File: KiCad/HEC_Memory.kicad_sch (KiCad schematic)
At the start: 11 parts, among them U13 74LS245, U14 74LS245, U15 74LS32, U16 74LS32, U2 AS6C4008-55PCN, U22 74LS02, U3 AS6C4008-55PCN, U4 CY7C199, U41 74LS02, U5 CY7C199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

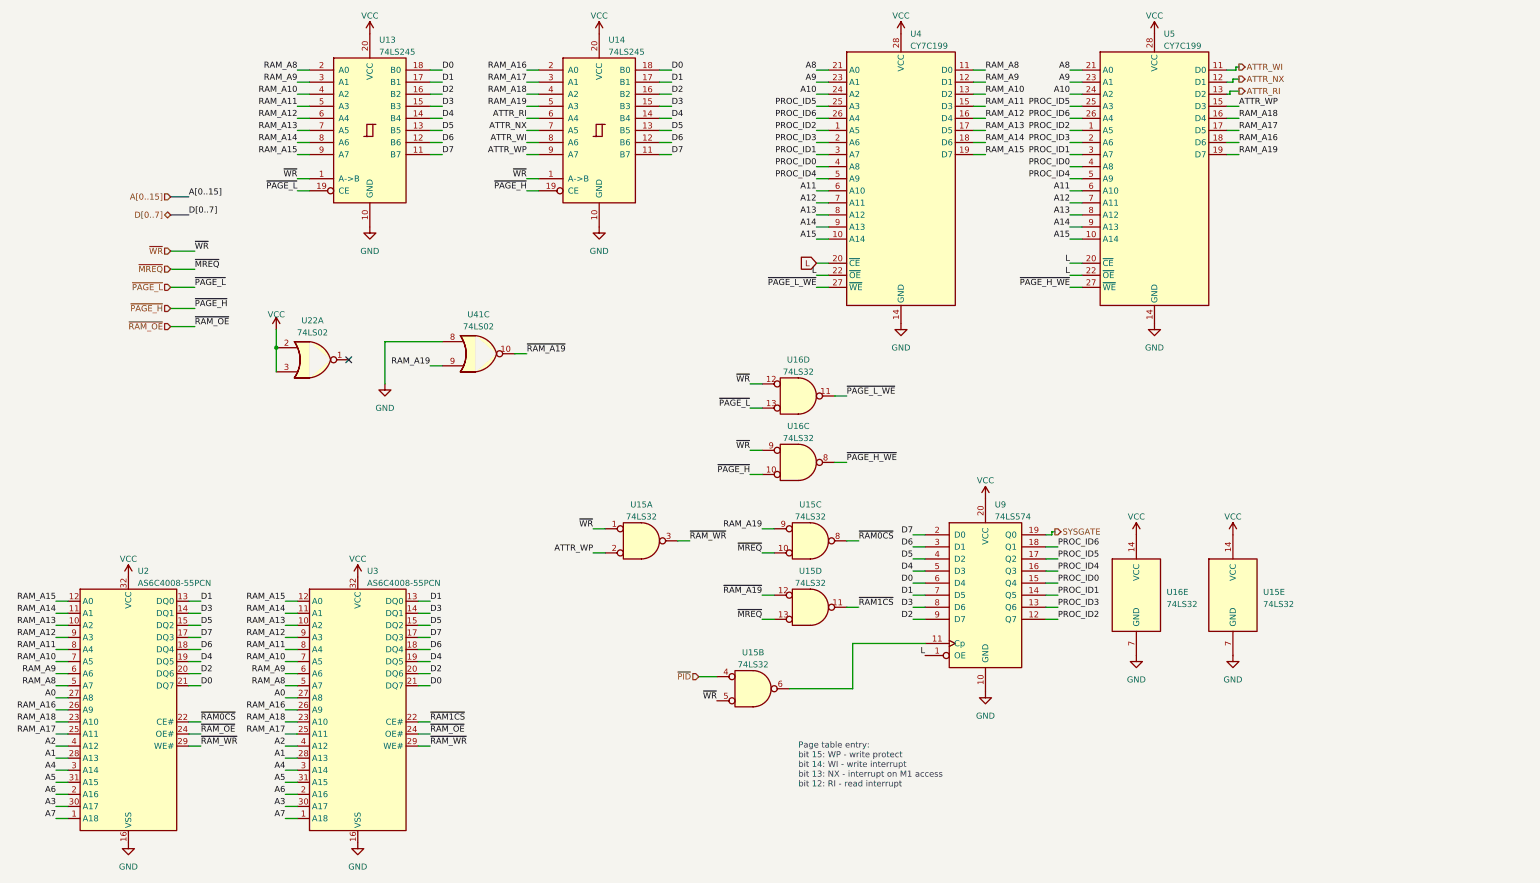
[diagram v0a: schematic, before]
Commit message: Bottom left routing complete
Finished routing the bottom left side of the PCB (wait generation and part of protection). Minor changes to schematic to ease routing.
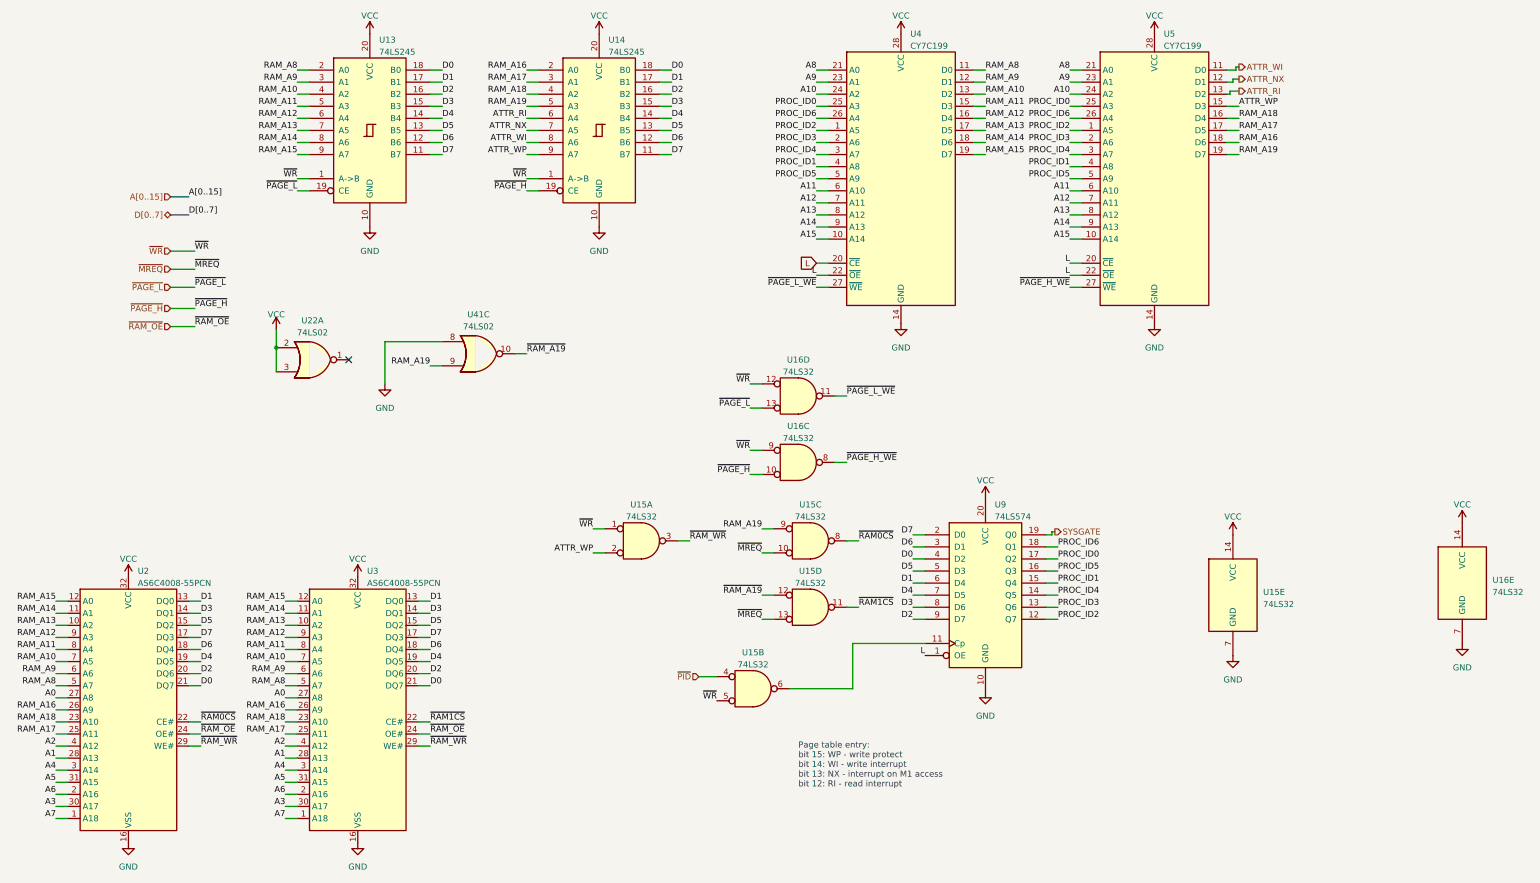
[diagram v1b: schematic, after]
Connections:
- net D0: now also U9.4 (D2); no longer U9.6 (D4)
- net D1: now also U9.6 (D4); no longer U9.7 (D5)
- net D4: now also U9.7 (D5); no longer U9.5 (D3)
- net D5: now also U9.5 (D3); no longer U9.4 (D2)
- net PROC_ID0: now also U4.25 (A3), U5.25 (A3), U9.17 (Q2); no longer U4.4 (A8), U5.4 (A8), U9.15 (Q4)
- net PROC_ID1: now also U4.4 (A8), U5.4 (A8), U9.15 (Q4); no longer U4.3 (A7), U5.3 (A7), U9.14 (Q5)
- net PROC_ID4: now also U4.3 (A7), U5.3 (A7), U9.14 (Q5); no longer U4.5 (A9), U5.5 (A9), U9.16 (Q3)
- net PROC_ID5: now also U4.5 (A9), U5.5 (A9), U9.16 (Q3); no longer U4.25 (A3), U5.25 (A3), U9.17 (Q2)
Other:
- moved on the sheet: U16E
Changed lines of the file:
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@@
     (effects (font (size 1.27 1.27)) (justify left bottom))
   )
-  (label "D4" (at 203.2 133.35 180) (fields_autoplaced)
+  (label "D4" (at 203.2 138.43 180) (fields_autoplaced)
     (effects (font (size 1.27 1.27)) (justify right bottom))
   )
@@
     (effects (font (size 1.27 1.27)) (justify right bottom))
   )
-  (label "D1" (at 203.2 138.43 180) (fields_autoplaced)
+  (label "D1" (at 203.2 135.89 180) (fields_autoplaced)
     (effects (font (size 1.27 1.27)) (justify right bottom))
   )
@@
     (effects (font (size 1.27 1.27)) (justify right bottom))
   )
-  (label "PROC_ID1" (at 233.68 138.43 0) (fields_autoplaced)
+  (label "PROC_ID1" (at 233.68 135.89 0) (fields_autoplaced)
     (effects (font (size 1.27 1.27)) (justify left bottom))
   )
@@
     (effects (font (size 1.27 1.27)) (justify left bottom))
   )
-  (label "PROC_ID4" (at 233.68 133.35 0) (fields_autoplaced)
+  (label "PROC_ID4" (at 233.68 138.43 0) (fields_autoplaced)
     (effects (font (size 1.27 1.27)) (justify left bottom))
   )
@@
     (effects (font (size 1.27 1.27)) (justify left bottom))
   )
-  (label "PROC_ID5" (at 233.68 130.81 0) (fields_autoplaced)
+  (label "PROC_ID5" (at 233.68 133.35 0) (fields_autoplaced)
     (effects (font (size 1.27 1.27)) (justify left bottom))
   )
@@
     (effects (font (size 1.27 1.27)) (justify right bottom))
   )
-  (label "PROC_ID5" (at 236.22 35.56 180) (fields_autoplaced)
+  (label "PROC_ID5" (at 236.22 50.8 180) (fields_autoplaced)
     (effects (font (size 1.27 1.27)) (justify right bottom))
   )
@@
     (effects (font (size 1.27 1.27)) (justify right bottom))
   )
-  (label "PROC_ID4" (at 236.22 50.8 180) (fields_autoplaced)
+  (label "PROC_ID4" (at 236.22 45.72 180) (fields_autoplaced)
     (effects (font (size 1.27 1.27)) (justify right bottom))
   )
@@
     (effects (font (size 1.27 1.27)) (justify left bottom))
   )
-  (label "D0" (at 203.2 135.89 180) (fields_autoplaced)
+  (label "D0" (at 203.2 130.81 180) (fields_autoplaced)
     (effects (font (size 1.27 1.27)) (justify right bottom))
   )
@@
     (effects (font (size 1.27 1.27)) (justify right bottom))
   )
-  (label "PROC_ID1" (at 236.22 45.72 180) (fields_autoplaced)
+  (label "PROC_ID1" (at 236.22 48.26 180) (fields_autoplaced)
     (effects (font (size 1.27 1.27)) (justify right bottom))
   )
@@
     (effects (font (size 1.27 1.27)) (justify left bottom))
   )
-  (label "PROC_ID1" (at 182.88 45.72 180) (fields_autoplaced)
+  (label "PROC_ID1" (at 182.88 48.26 180) (fields_autoplaced)
     (effects (font (size 1.27 1.27)) (justify right bottom))
   )
@@
     (effects (font (size 1.27 1.27)) (justify right bottom))
   )
-  (label "PROC_ID5" (at 182.88 35.56 180) (fields_autoplaced)
+  (label "PROC_ID5" (at 182.88 50.8 180) (fields_autoplaced)
     (effects (font (size 1.27 1.27)) (justify right bottom))
   )
@@
     (effects (font (size 1.27 1.27)) (justify right bottom))
   )
-  (label "PROC_ID0" (at 236.22 48.26 180) (fields_autoplaced)
+  (label "PROC_ID0" (at 236.22 35.56 180) (fields_autoplaced)
     (effects (font (size 1.27 1.27)) (justify right bottom))
   )
@@
     (effects (font (size 1.27 1.27)) (justify left bottom))
   )
-  (label "PROC_ID4" (at 182.88 50.8 180) (fields_autoplaced)
+  (label "PROC_ID4" (at 182.88 45.72 180) (fields_autoplaced)
     (effects (font (size 1.27 1.27)) (justify right bottom))
   )
@@
     (effects (font (size 1.27 1.27)) (justify right bottom))
   )
-  (label "PROC_ID0" (at 233.68 135.89 0) (fields_autoplaced)
+  (label "PROC_ID0" (at 233.68 130.81 0) (fields_autoplaced)
     (effects (font (size 1.27 1.27)) (justify left bottom))
   )
@@
     (effects (font (size 1.27 1.27)) (justify left bottom))
   )
-  (label "PROC_ID0" (at 182.88 48.26 180) (fields_autoplaced)
-    (effects (font (size 1.27 1.27)) (justify right bottom))
-  )
-  (label "D5" (at 203.2 130.81 180) (fields_autoplaced)
+  (label "PROC_ID0" (at 182.88 35.56 180) (fields_autoplaced)
+    (effects (font (size 1.27 1.27)) (justify right bottom))
+  )
+  (label "D5" (at 203.2 133.35 180) (fields_autoplaced)
     (effects (font (size 1.27 1.27)) (justify right bottom))
   )
@@
     )
   )
-  (symbol (lib_id "power:GND") (at 250.19 151.13 0) (unit 1)
-    (in_bom yes) (on_board yes) (dnp no) (fields_autoplaced)
-    (property "Reference" "#PWR022" (at 250.19 157.48 0)
-      (effects (font (size 1.27 1.27)) hide)
-    )
-    (property "Value" "GND" (at 250.19 156.21 0)
-      (effects (font (size 1.27 1.27)))
-    )
-    (property "Footprint" "" (at 250.19 151.13 0)
-      (effects (font (size 1.27 1.27)) hide)
-    )
-    (property "Datasheet" "" (at 250.19 151.13 0)
+  (symbol (lib_id "power:GND") (at 318.77 148.59 0) (unit 1)
+    (in_bom yes) (on_board yes) (dnp no) (fields_autoplaced)
+    (property "Reference" "#PWR022" (at 318.77 154.94 0)
+      (effects (font (size 1.27 1.27)) hide)
+    )
+    (property "Value" "GND" (at 318.77 153.67 0)
+      (effects (font (size 1.27 1.27)))
+    )
+    (property "Footprint" "" (at 318.77 148.59 0)
+      (effects (font (size 1.27 1.27)) hide)
+    )
+    (property "Datasheet" "" (at 318.77 148.59 0)
       (effects (font (size 1.27 1.27)) hide)
     )
@@
     )
   )
-  (symbol (lib_id "power:VCC") (at 250.19 125.73 0) (unit 1)
-    (in_bom yes) (on_board yes) (dnp no) (fields_autoplaced)
-    (property "Reference" "#PWR021" (at 250.19 129.54 0)
-      (effects (font (size 1.27 1.27)) hide)
-    )
-    (property "Value" "VCC" (at 250.19 121.92 0)
-      (effects (font (size 1.27 1.27)))
-    )
-    (property "Footprint" "" (at 250.19 125.73 0)
-      (effects (font (size 1.27 1.27)) hide)
-    )
-    (property "Datasheet" "" (at 250.19 125.73 0)
+  (symbol (lib_id "power:VCC") (at 318.77 123.19 0) (unit 1)
+    (in_bom yes) (on_board yes) (dnp no) (fields_autoplaced)
+    (property "Reference" "#PWR021" (at 318.77 127 0)
+      (effects (font (size 1.27 1.27)) hide)
+    )
+    (property "Value" "VCC" (at 318.77 119.38 0)
+      (effects (font (size 1.27 1.27)))
+    )
+    (property "Footprint" "" (at 318.77 123.19 0)
+      (effects (font (size 1.27 1.27)) hide)
+    )
+    (property "Datasheet" "" (at 318.77 123.19 0)
       (effects (font (size 1.27 1.27)) hide)
     )
@@
     )
   )
-  (symbol (lib_id "74xx:74LS32") (at 250.19 138.43 0) (unit 5)
-    (in_bom yes) (on_board yes) (dnp no) (fields_autoplaced)
-    (property "Reference" "U16" (at 256.54 137.795 0)
+  (symbol (lib_id "74xx:74LS32") (at 318.77 135.89 0) (unit 5)
+    (in_bom yes) (on_board yes) (dnp no) (fields_autoplaced)
+    (property "Reference" "U16" (at 325.12 135.255 0)
       (effects (font (size 1.27 1.27)) (justify left))
     )
-    (property "Value" "74LS32" (at 256.54 140.335 0)
+    (property "Value" "74LS32" (at 325.12 137.795 0)
       (effects (font (size 1.27 1.27)) (justify left))
     )
-    (property "Footprint" "Package_DIP:DIP-14_W7.62mm_Socket" (at 250.19 138.43 0)
-      (effects (font (size 1.27 1.27)) hide)
-    )
-    (property "Datasheet" "http://www.ti.com/lit/gpn/sn74LS32" (at 250.19 138.43 0)
-      (effects (font (size 1.27 1.27)) hide)
-    )
+    (property "Footprint" "Package_DIP:DIP-14_W7.62mm_Socket" (at 318.77 135.89 0)
+      (effects (font (size 1.27 1.27)) hide)
+    )
+    (property "Datasheet" "http://www.ti.com/lit/gpn/sn74LS32" (at 318.77 135.89 0)
+      (effects (font (size 1.27 1.27)) hide)
+    )

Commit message: Preliminary routing
Changed footprint pad size to allow 2 traces to be routed between adjacent pads. Finished routing all ICs. Bypass caps not added. Some traces may need to be optimized.
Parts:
- U13, U14, U9: footprint Package_DIP:DIP-20_W7.62mm_Socket -> Library:DIP-20_W7.62mm_Socket_ThinPads
- U15, U16, U22, U41: footprint Package_DIP:DIP-14_W7.62mm_Socket -> Library:DIP-14_W7.62mm_Socket_ThinPads
- U2, U3: footprint Package_DIP:DIP-32_W15.24mm_Socket -> Library:DIP-32_W15.24mm_Socket_ThinPads
- U4, U5: footprint Package_DIP:DIP-28_W7.62mm_Socket -> Library:DIP-28_W7.62mm_Socket_ThinPads
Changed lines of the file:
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@@
       (effects (font (size 1.27 1.27)) (justify left))
     )
-    (property "Footprint" "Package_DIP:DIP-14_W7.62mm_Socket" (at 270.51 138.43 0)
+    (property "Footprint" "Library:DIP-14_W7.62mm_Socket_ThinPads" (at 270.51 138.43 0)
       (effects (font (size 1.27 1.27)) hide)
     )
@@
       (effects (font (size 1.27 1.27)) (justify left))
     )
-    (property "Footprint" "Package_DIP:DIP-32_W15.24mm_Socket" (at 38.1 160.02 0)
+    (property "Footprint" "Library:DIP-32_W15.24mm_Socket_ThinPads" (at 38.1 160.02 0)
       (effects (font (size 1.27 1.27)) hide)
     )
@@
       (effects (font (size 1.27 1.27)))
     )
-    (property "Footprint" "Package_DIP:DIP-14_W7.62mm_Socket" (at 179.07 96.52 0)
+    (property "Footprint" "Library:DIP-14_W7.62mm_Socket_ThinPads" (at 179.07 96.52 0)
       (effects (font (size 1.27 1.27)) hide)
     )
@@
       (effects (font (size 1.27 1.27)) (justify left))
     )
-    (property "Footprint" "Package_DIP:DIP-28_W7.62mm_Socket" (at 200.66 50.8 0)
+    (property "Footprint" "Library:DIP-28_W7.62mm_Socket_ThinPads" (at 200.66 50.8 0)
       (effects (font (size 1.27 1.27)) hide)
     )
@@
       (effects (font (size 1.27 1.27)))
     )
-    (property "Footprint" "Package_DIP:DIP-14_W7.62mm_Socket" (at 179.07 110.49 0)
+    (property "Footprint" "Library:DIP-14_W7.62mm_Socket_ThinPads" (at 179.07 110.49 0)
       (effects (font (size 1.27 1.27)) hide)
     )
@@
       (effects (font (size 1.27 1.27)) (justify left))
     )
-    (property "Footprint" "Package_DIP:DIP-32_W15.24mm_Socket" (at 86.36 160.02 0)
+    (property "Footprint" "Library:DIP-32_W15.24mm_Socket_ThinPads" (at 86.36 160.02 0)
       (effects (font (size 1.27 1.27)) hide)
     )
@@
       (effects (font (size 1.27 1.27)) (justify left))
     )
-    (property "Footprint" "Package_DIP:DIP-28_W7.62mm_Socket" (at 254 50.8 0)
+    (property "Footprint" "Library:DIP-28_W7.62mm_Socket_ThinPads" (at 254 50.8 0)
       (effects (font (size 1.27 1.27)) hide)
     )
@@
       (effects (font (size 1.27 1.27)))
     )
-    (property "Footprint" "Package_DIP:DIP-14_W7.62mm_Socket" (at 76.835 88.9 0)
+    (property "Footprint" "Library:DIP-14_W7.62mm_Socket_ThinPads" (at 76.835 88.9 0)
       (effects (font (size 1.27 1.27)) hide)
     )
@@
       (effects (font (size 1.27 1.27)))
     )
-    (property "Footprint" "Package_DIP:DIP-14_W7.62mm_Socket" (at 181.61 127 0)
+    (property "Footprint" "Library:DIP-14_W7.62mm_Socket_ThinPads" (at 181.61 127 0)
       (effects (font (size 1.27 1.27)) hide)
     )
@@
       (effects (font (size 1.27 1.27)))
     )
-    (property "Footprint" "Package_DIP:DIP-14_W7.62mm_Socket" (at 169.545 158.115 0)
+    (property "Footprint" "Library:DIP-14_W7.62mm_Socket_ThinPads" (at 169.545 158.115 0)
       (effects (font (size 1.27 1.27)) hide)
     )
@@
       (effects (font (size 1.27 1.27)))
     )
-    (property "Footprint" "Package_DIP:DIP-14_W7.62mm_Socket" (at 111.76 87.63 0)
+    (property "Footprint" "Library:DIP-14_W7.62mm_Socket_ThinPads" (at 111.76 87.63 0)
       (effects (font (size 1.27 1.27)) hide)
     )
@@
       (effects (font (size 1.27 1.27)) (justify left))
     )
-    (property "Footprint" "Package_DIP:DIP-20_W7.62mm_Socket" (at 137.16 40.64 0)
+    (property "Footprint" "Library:DIP-20_W7.62mm_Socket_ThinPads" (at 137.16 40.64 0)
       (effects (font (size 1.27 1.27)) hide)
     )
@@
       (effects (font (size 1.27 1.27)))
     )
-    (property "Footprint" "Package_DIP:DIP-14_W7.62mm_Socket" (at 181.61 140.97 0)
+    (property "Footprint" "Library:DIP-14_W7.62mm_Socket_ThinPads" (at 181.61 140.97 0)
       (effects (font (size 1.27 1.27)) hide)
     )
@@
       (effects (font (size 1.27 1.27)) (justify left))
     )
-    (property "Footprint" "Package_DIP:DIP-20_W7.62mm_Socket" (at 88.9 40.64 0)
+    (property "Footprint" "Library:DIP-20_W7.62mm_Socket_ThinPads" (at 88.9 40.64 0)
       (effects (font (size 1.27 1.27)) hide)
     )
@@
       (effects (font (size 1.27 1.27)) (justify left))
     )
-    (property "Footprint" "Package_DIP:DIP-20_W7.62mm_Socket" (at 218.44 138.43 0)
+    (property "Footprint" "Library:DIP-20_W7.62mm_Socket_ThinPads" (at 218.44 138.43 0)
       (effects (font (size 1.27 1.27)) hide)
     )
@@
       (effects (font (size 1.27 1.27)))
     )
-    (property "Footprint" "Package_DIP:DIP-14_W7.62mm_Socket" (at 146.05 127 0)
+    (property "Footprint" "Library:DIP-14_W7.62mm_Socket_ThinPads" (at 146.05 127 0)
       (effects (font (size 1.27 1.27)) hide)
     )
@@
       (effects (font (size 1.27 1.27)) (justify left))
     )
-    (property "Footprint" "Package_DIP:DIP-14_W7.62mm_Socket" (at 318.77 135.89 0)
-      (effects (font (size 1.27 1.27)) hide)
-    )
+    (property "Footprint" "Library:DIP-14_W7.62mm_Socket_ThinPads" (at 318.77 135.89 0)
+      (effects (font (size 1.27 1.27)) hide)
+    )

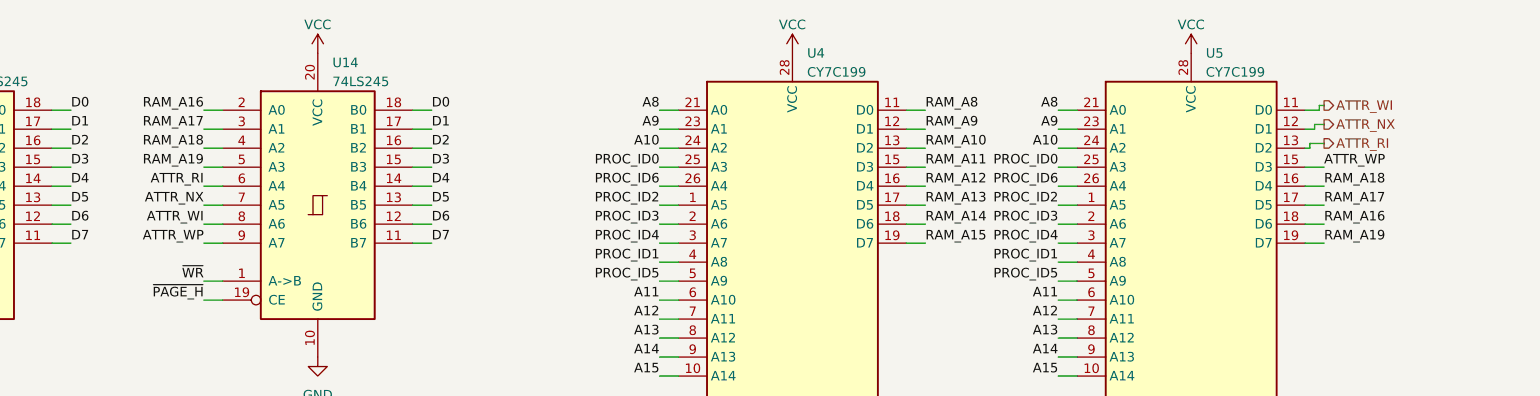
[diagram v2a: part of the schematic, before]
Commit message: change NX bit to XE bit
change No eXecute to eXecute Enable (inverting the polarity of the signal) in order to fix a bug that causes the HEC to not recognize a NX when the instruction fetched is a RST.
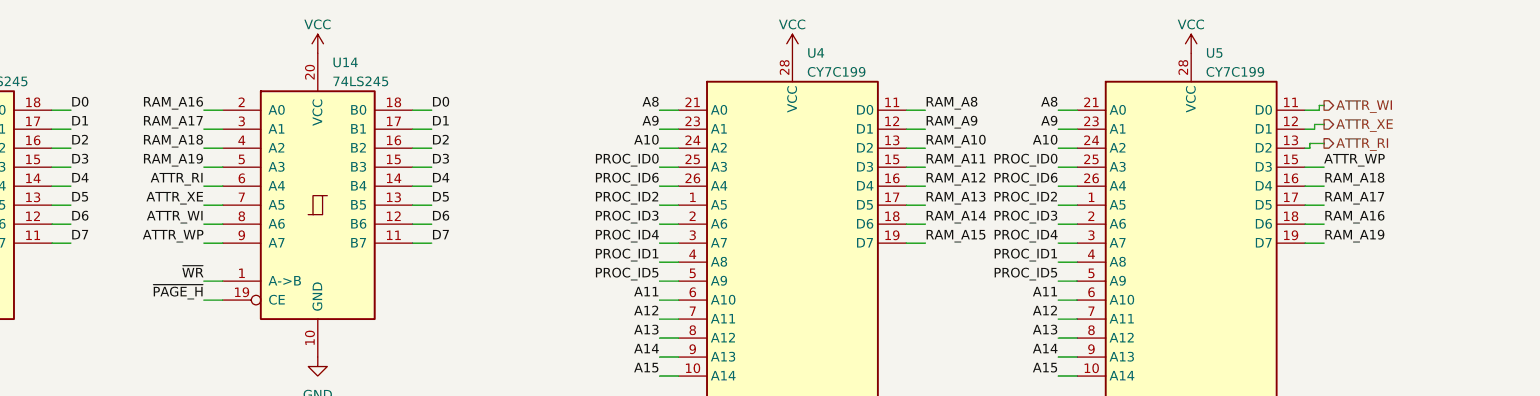
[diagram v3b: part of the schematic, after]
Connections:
- net ATTR_NX renamed ATTR_XE
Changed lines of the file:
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@@
     (effects (font (size 1.27 1.27)) (justify right bottom))
   )
-  (label "ATTR_NX" (at 121.92 40.64 180) (fields_autoplaced)
+  (label "ATTR_XE" (at 121.92 40.64 180) (fields_autoplaced)
     (effects (font (size 1.27 1.27)) (justify right bottom))
   )
@@
     (effects (font (size 1.27 1.27)) (justify left))
   )
-  (hierarchical_label "ATTR_NX" (shape output) (at 271.78 29.845 0) (fields_autoplaced)
+  (hierarchical_label "ATTR_XE" (shape output) (at 271.78 29.845 0) (fields_autoplaced)
     (effects (font (size 1.27 1.27)) (justify left))
   )
